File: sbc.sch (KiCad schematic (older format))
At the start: 1 part

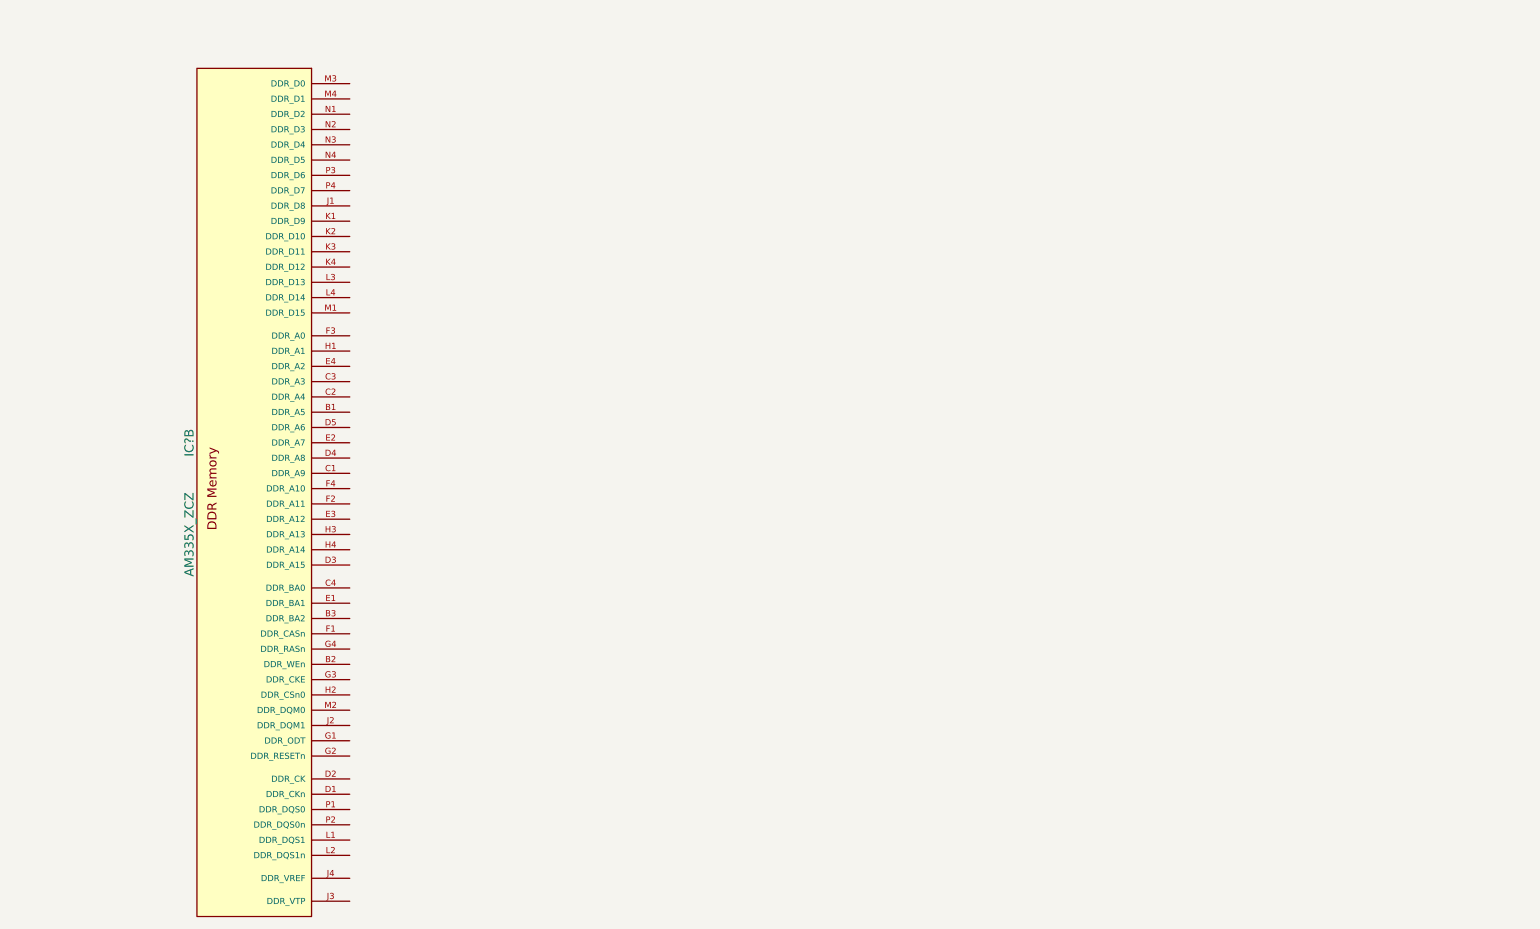
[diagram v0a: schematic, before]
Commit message: Connected micro SD
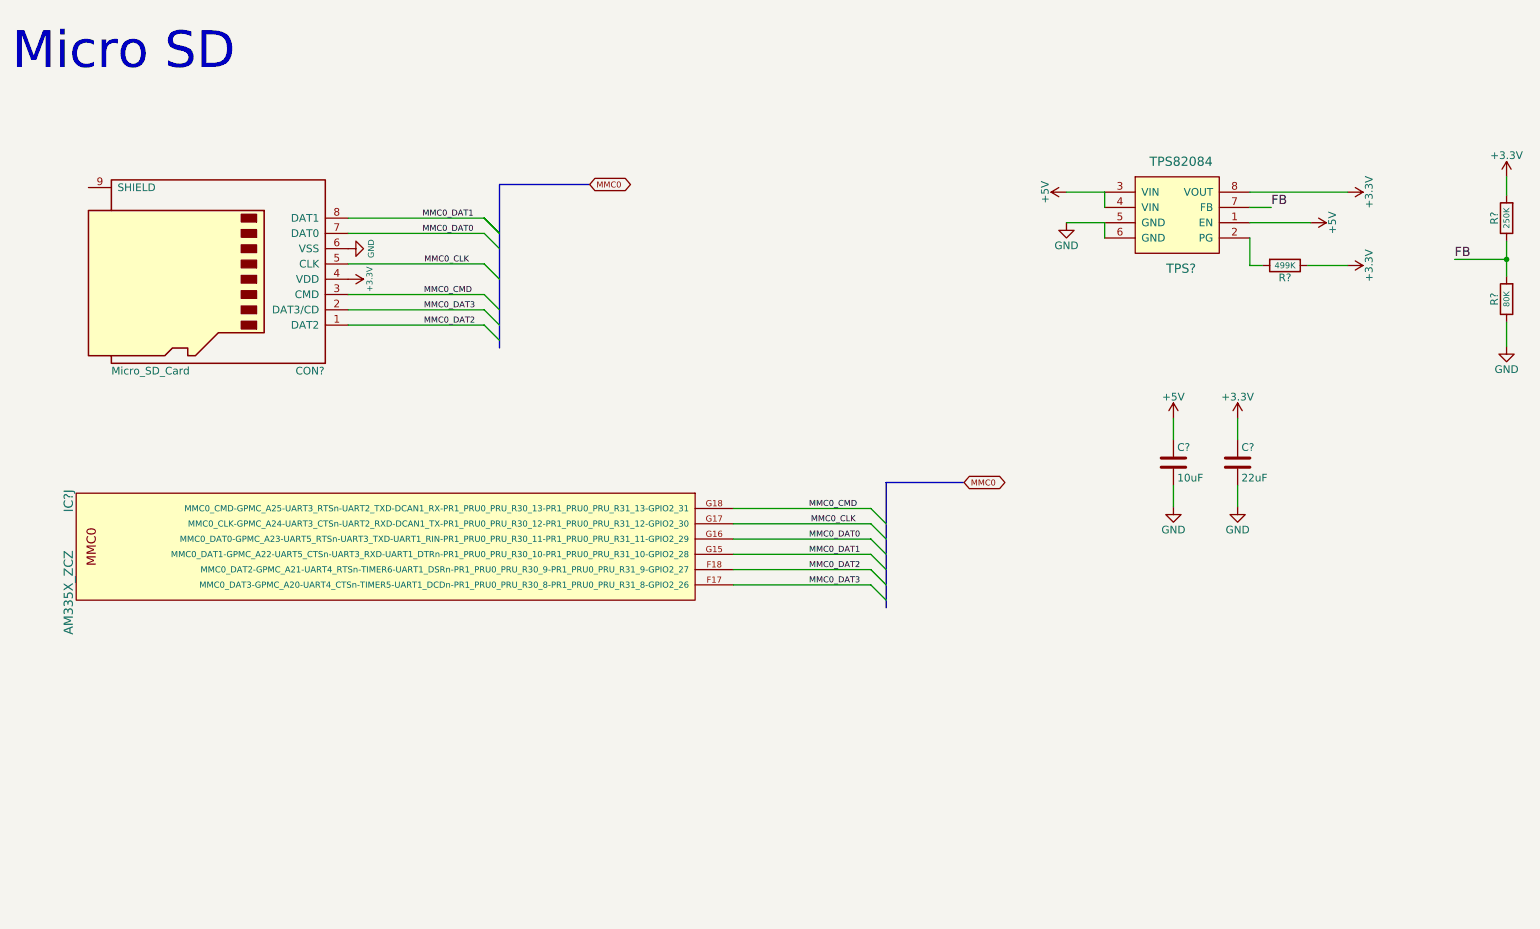
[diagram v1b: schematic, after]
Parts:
- removed IC?: AM335X_ZCZ, symbol AM335X_ZCZ
- added C?: 10uF, symbol C
- added C?: 22uF, symbol C
- added CON?: Micro_SD_Card, symbol Micro_SD_Card
- added IC?: AM335X_ZCZ, symbol AM335X_ZCZ
- added R?: 499K, symbol R
- added R?: 250K, symbol R
- added R?: 80K, symbol R
- added TPS?: TPS82084, symbol TPS82084
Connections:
- new net: R?.2, TPS?.2 (PG)
- new net +3V3: C?.1, CON?.4 (VDD), R?.1, R?.2, TPS?.8 (VOUT)
- new net +5V: C?.1, TPS?.1 (EN), TPS?.3 (VIN), TPS?.4 (VIN)
- new net FB: R?.1, R?.2, TPS?.7 (FB)
- new net GND: C?.2, C?.2, CON?.6 (VSS), R?.1, TPS?.5 (GND), TPS?.6 (GND)
- new net MMC0_CLK: CON?.5 (CLK), IC?.G17 (MMC0_CLK-GPMC_A24-UART3_CTSn-UART2_RXD-DCAN1_TX-PR1_PRU0_PRU_R30_12-PR1_PRU0_PRU_R31_12-GPIO2_30)
- new net MMC0_CMD: CON?.3 (CMD), IC?.G18 (MMC0_CMD-GPMC_A25-UART3_RTSn-UART2_TXD-DCAN1_RX-PR1_PRU0_PRU_R30_13-PR1_PRU0_PRU_R31_13-GPIO2_31)
- new net MMC0_DAT0: CON?.7 (DAT0), IC?.G16 (MMC0_DAT0-GPMC_A23-UART5_RTSn-UART3_TXD-UART1_RIN-PR1_PRU0_PRU_R30_11-PR1_PRU0_PRU_R31_11-GPIO2_29)
- new net MMC0_DAT1: CON?.8 (DAT1), IC?.G15 (MMC0_DAT1-GPMC_A22-UART5_CTSn-UART3_RXD-UART1_DTRn-PR1_PRU0_PRU_R30_10-PR1_PRU0_PRU_R31_10-GPIO2_28)
- new net MMC0_DAT2: CON?.1 (DAT2), IC?.F18 (MMC0_DAT2-GPMC_A21-UART4_RTSn-TIMER6-UART1_DSRn-PR1_PRU0_PRU_R30_9-PR1_PRU0_PRU_R31_9-GPIO2_27)
- new net MMC0_DAT3: CON?.2 (DAT3/CD), IC?.F17 (MMC0_DAT3-GPMC_A20-UART4_CTSn-TIMER5-UART1_DCDn-PR1_PRU0_PRU_R30_8-PR1_PRU0_PRU_R31_8-GPIO2_26)
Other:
- note added: "Micro SD"

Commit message: Connected RAM
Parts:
- added C?: 10uF, symbol C
- added C?: 22uF, symbol C
- added CON?: Micro_SD_Card, symbol Micro_SD_Card
- added DRAM?: DRAM-IS43TR16128B-125KBL, symbol DRAM-IS43TR16128B-125KBL
- added IC? (x2): AM335X_ZCZ, symbol AM335X_ZCZ
- added R?: 499K, symbol R
- added R?: 250K, symbol R
- added R?: 80K, symbol R
- added R?: 49.9, symbol R
- added TPS?: TPS82084, symbol TPS82084
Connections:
- net +3V3: now also C?.1, CON?.4 (VDD), R?.1, R?.2, TPS?.8 (VOUT)
- net +5V: now also C?.1, TPS?.1 (EN), TPS?.3 (VIN), TPS?.4 (VIN)
- net FB: now also R?.1, R?.2, TPS?.7 (FB)
- net GND: now also C?.2, C?.2, CON?.6 (VSS), DRAM?.B1 (VSSQ), DRAM?.E1 (VSS), DRAM?.G9 (VSSQ), DRAM?.T9 (VSS), R?.1, R?.2, TPS?.5 (GND), TPS?.6 (GND)
- net MMC0_CLK: now also CON?.5 (CLK), IC?.G17 (MMC0_CLK-GPMC_A24-UART3_CTSn-UART2_RXD-DCAN1_TX-PR1_PRU0_PRU_R30_12-PR1_PRU0_PRU_R31_12-GPIO2_30)
- net MMC0_CMD: now also CON?.3 (CMD), IC?.G18 (MMC0_CMD-GPMC_A25-UART3_RTSn-UART2_TXD-DCAN1_RX-PR1_PRU0_PRU_R30_13-PR1_PRU0_PRU_R31_13-GPIO2_31)
- net MMC0_DAT0: now also CON?.7 (DAT0), IC?.G16 (MMC0_DAT0-GPMC_A23-UART5_RTSn-UART3_TXD-UART1_RIN-PR1_PRU0_PRU_R30_11-PR1_PRU0_PRU_R31_11-GPIO2_29)
- net MMC0_DAT1: now also CON?.8 (DAT1), IC?.G15 (MMC0_DAT1-GPMC_A22-UART5_CTSn-UART3_RXD-UART1_DTRn-PR1_PRU0_PRU_R30_10-PR1_PRU0_PRU_R31_10-GPIO2_28)
- net MMC0_DAT2: now also CON?.1 (DAT2), IC?.F18 (MMC0_DAT2-GPMC_A21-UART4_RTSn-TIMER6-UART1_DSRn-PR1_PRU0_PRU_R30_9-PR1_PRU0_PRU_R31_9-GPIO2_27)
- net MMC0_DAT3: now also CON?.2 (DAT3/CD), IC?.F17 (MMC0_DAT3-GPMC_A20-UART4_CTSn-TIMER5-UART1_DCDn-PR1_PRU0_PRU_R30_8-PR1_PRU0_PRU_R31_8-GPIO2_26)
- net at CON?.9 (SHIELD): now also CON?.9 (SHIELD)
- net at R?.2, TPS?.2 (PG): now also R?.2, TPS?.2 (PG)
- new net: IC?.J3 (DDR_VTP), R?.1
- new net +1.5V: DRAM?.A1 (VDDQ), DRAM?.H9 (VDDQ), DRAM?.N1 (VDD), DRAM?.R9 (VDD)
- new net DDR_A0: DRAM?.N3 (A0), IC?.F3 (DDR_A0)
- new net DDR_A1: DRAM?.P7 (A1), IC?.H1 (DDR_A1)
- new net DDR_A10: DRAM?.L7 (A10/AP), IC?.F4 (DDR_A10)
- new net DDR_A11: DRAM?.R7 (A11), IC?.F2 (DDR_A11)
- new net DDR_A12: DRAM?.N7 (A12/BC#), IC?.E3 (DDR_A12)
- new net DDR_A13: DRAM?.T3 (A13), IC?.H3 (DDR_A13)
- new net DDR_A2: DRAM?.P3 (A2), IC?.E4 (DDR_A2)
- new net DDR_A3: DRAM?.N2 (A3), IC?.C3 (DDR_A3)
- new net DDR_A4: DRAM?.P8 (A4), IC?.C2 (DDR_A4)
- new net DDR_A5: DRAM?.P2 (A5), IC?.B1 (DDR_A5)
- new net DDR_A6: DRAM?.R8 (A6), IC?.D5 (DDR_A6)
- new net DDR_A7: DRAM?.R2 (A7), IC?.E2 (DDR_A7)
- new net DDR_A8: DRAM?.T8 (A8), IC?.D4 (DDR_A8)
- new net DDR_A9: DRAM?.R3 (A9), IC?.C1 (DDR_A9)
- new net DDR_BA0: DRAM?.M2 (BA0), IC?.C4 (DDR_BA0)
- new net DDR_BA1: DRAM?.N8 (BA1), IC?.E1 (DDR_BA1)
- new net DDR_BA2: DRAM?.M3 (BA2), IC?.B3 (DDR_BA2)
- new net DDR_CASn: DRAM?.K3 (CAS#), IC?.F1 (DDR_CASn)
- new net DDR_CK: DRAM?.J7 (CK), IC?.D2 (DDR_CK)
- new net DDR_CKE: DRAM?.K9 (CKE), IC?.G3 (DDR_CKE)
- new net DDR_CKn: DRAM?.K7 (CK#), IC?.D1 (DDR_CKn)
- new net DDR_CSn0: DRAM?.L2 (CS#), IC?.H2 (DDR_CSn0)
- new net DDR_D0: DRAM?.E3 (DQL0), IC?.M3 (DDR_D0)
- new net DDR_D1: DRAM?.F7 (DQL1), IC?.M4 (DDR_D1)
- new net DDR_D10: DRAM?.C8 (DQU2), IC?.K2 (DDR_D10)
- new net DDR_D11: DRAM?.C2 (DQU3), IC?.K3 (DDR_D11)
- new net DDR_D12: DRAM?.A7 (DQU4), IC?.K4 (DDR_D12)
- new net DDR_D13: DRAM?.A2 (DQU5), IC?.L3 (DDR_D13)
- new net DDR_D14: DRAM?.B8 (DQU6), IC?.L4 (DDR_D14)
- new net DDR_D15: DRAM?.A3 (DQU7), IC?.M1 (DDR_D15)
- new net DDR_D2: DRAM?.F2 (DQL2), IC?.N1 (DDR_D2)
- new net DDR_D3: DRAM?.F8 (DQL3), IC?.N2 (DDR_D3)
- new net DDR_D4: DRAM?.H3 (DQL4), IC?.N3 (DDR_D4)
- new net DDR_D5: DRAM?.H8 (DQL5), IC?.N4 (DDR_D5)
- new net DDR_D6: DRAM?.G2 (DQL6), IC?.P3 (DDR_D6)
- new net DDR_D7: DRAM?.H7 (DQL7), IC?.P4 (DDR_D7)
- new net DDR_D8: DRAM?.D7 (DQU0), IC?.J1 (DDR_D8)
- new net DDR_D9: DRAM?.C3 (DQU1), IC?.K1 (DDR_D9)
- new net DDR_DQM0: DRAM?.E7 (DML), IC?.M2 (DDR_DQM0)
- new net DDR_DQM1: DRAM?.D3 (DMU), IC?.J2 (DDR_DQM1)
- new net DDR_DQS0: DRAM?.F3 (DQSL), IC?.P1 (DDR_DQS0)
- new net DDR_DQS1: DRAM?.C7 (DQSU), IC?.L1 (DDR_DQS1)
- new net DDR_DQSn0: DRAM?.G3 (DQSL#), IC?.P2 (DDR_DQS0n)
- new net DDR_DQSn1: DRAM?.B7 (DQSU#), IC?.L2 (DDR_DQS1n)
- new net DDR_ODT: DRAM?.K1 (ODT), IC?.G1 (DDR_ODT)
- new net DDR_RASn: DRAM?.J3 (RAS#), IC?.G4 (DDR_RASn)
- new net DDR_RESETn: DRAM?.T2 (RESET#), IC?.G2 (DDR_RESETn)
- new net DDR_VREF: DRAM?.H1 (VREFDQ), DRAM?.M8 (VREFCA), IC?.J4 (DDR_VREF)
- new net DDR_WEn: DRAM?.L3 (WE#), IC?.B2 (DDR_WEn)
- new net DDR_ZQ: DRAM?.L8 (ZQ)
- no-connect marks 0 -> 8
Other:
- moved on the sheet: C?, CON?, IC?J, R?, TPS?

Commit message: Added Power, USB, System
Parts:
- removed C? (x2): 10uF, symbol C
- removed C? (x2): 22uF, symbol C
- removed CON?: Micro_SD_Card, symbol Micro_SD_Card
- removed IC?: AM335X_ZCZ, symbol AM335X_ZCZ
- removed R? (x2): 499K, symbol R
- removed R? (x2): 250K, symbol R
- removed R? (x2): 80K, symbol R
- removed TPS? (x2): TPS82084, symbol TPS82084
- added C? (x4): 0.1uF, symbol C
- added C? (x3): 10uF, symbol C
- added C? (x3): 22uF, symbol C
- added C? (x2): 24pF, symbol C
- added C? (x2): 25pF, symbol C
- added C? (x4): 1uF, symbol C
- added F?: Polyfuse, symbol Polyfuse
- added IC? (x3): AM335X_ZCZ, symbol AM335X_ZCZ
- added L?: Ferrite_Bead, symbol Ferrite_Bead
- added P?: USB_A, symbol USB_A
- added R? (x2): 1K, symbol R
- added R? (x3): 499K, symbol R
- added R?: 70K, symbol R
- added R? (x3): 80K, symbol R
- added R?: 250K, symbol R
- added R?: 30K, symbol R
- added R?: 240, symbol R
- added R?: 1M, symbol R
- added R?: 10K, symbol R
- added TPS? (x3): TPS82084, symbol TPS82084
- added Y?: 24MHz, symbol Crystal
- added Y?: 32.768KHz, symbol Crystal
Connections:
- net +1.5V: now also C?.1, C?.1, R?.1, R?.1, R?.1, TPS?.8 (VOUT)
- net +3V3: now also C?.1, IC?.N15 (VDDA3P3V_USB0), IC?.R15 (xVDDA3P3V_USB1), R?.1, R?.1, TPS?.8 (VOUT)
- net +5V: now also C?.1, C?.1, C?.1, IC?.F16 (USB0_DRVVBUS-GPIO0_18), IC?.P15 (USB0_VBUS), L?.1, TPS?.1 (EN), TPS?.1 (EN), TPS?.1 (EN), TPS?.3 (VIN), TPS?.3 (VIN), TPS?.3 (VIN), TPS?.4 (VIN), TPS?.4 (VIN), TPS?.4 (VIN)
- net DDR_VREF: now also C?.1, C?.1, C?.1, C?.2, R?.1, R?.2
- net DDR_ZQ: now also R?.2
- net GND: now also C?.2, C?.2, C?.2, C?.2, C?.2, C?.2, C?.2, C?.2, C?.2, C?.2, C?.2, C?.2, C?.2, IC?.A1 (VSS), IC?.A18 (VSS), IC?.F8 (VSS), IC?.G11 (VSS), IC?.G12 (VSS), IC?.G8 (VSS), IC?.G9 (VSS), IC?.H10 (VSS), IC?.H12 (VSS), IC?.H6 (VSS), IC?.H7 (VSS), IC?.H8 (VSS), IC?.H9 (VSS), IC?.J10 (VSS), IC?.J11 (VSS), IC?.J6 (VSS), IC?.J7 (VSS), IC?.J8 (VSS), IC?.J9 (VSS), IC?.K10 (VSS), IC?.K11 (VSS), IC?.K7 (VSS), IC?.K9 (VSS), IC?.L10 (VSS), IC?.L11 (VSS), IC?.L12 (VSS), IC?.L13 (VSS), IC?.M10 (VSS), IC?.M12 (VSS), IC?.M14 (VSSA_USB), IC?.M6 (VSS), IC?.M7 (VSS), IC?.M8 (VSS), IC?.M9 (VSS), IC?.N10 (VSS), IC?.N11 (VSS), IC?.N14 (VSSA_USB), IC?.N7 (VSS), IC?.V1 (VSS), IC?.V18 (VSS), P?.4 (GND), R?.1, R?.2, R?.2, R?.2, R?.2, R?.2, TPS?.5 (GND), TPS?.5 (GND), TPS?.5 (GND), TPS?.6 (GND), TPS?.6 (GND), TPS?.6 (GND)
- new net: F?.2, P?.1 (VBUS)
- new net: C?.1, IC?.C10 (CAP_VBB_MPU)
- new net: C?.1, IC?.D11 (CAP_VDD_SRAM_MPU)
- new net: C?.1, IC?.D6 (CAP_VDD_RTC)
- new net: C?.1, IC?.D9 (CAP_VDD_SRAM_CORE)
- new net: F?.1, L?.2
- new net: R?.2, TPS?.2 (PG) (x3)
- new net: C?.1, IC?.A4 (RTC_XTALOUT), Y?.2
- new net: C?.1, IC?.A6 (RTC_XTALIN), Y?.1
- new net: IC?.B4 (RTC_KALDO_ENn), R?.1
- new net: C?.1, IC?.U11 (XTALOUT), R?.2, Y?.2
- new net: C?.1, IC?.V10 (XTALIN), R?.1, Y?.1
- new net 1.1FB: R?.1, R?.2, TPS?.7 (FB)
- new net 1.1V: C?.1, IC?.A2 (xVDD_MPU_MON), IC?.F10 (xVDD_MPU), IC?.F11 (xVDD_MPU), IC?.F12 (xVDD_MPU), IC?.F13 (xVDD_MPU), IC?.F6 (VDD_CORE), IC?.F7 (VDD_CORE), IC?.G10 (VDD_CORE), IC?.G13 (xVDD_MPU), IC?.G6 (VDD_CORE), IC?.G7 (VDD_CORE), IC?.H11 (VDD_CORE), IC?.H13 (xVDD_MPU), IC?.J12 (VDD_CORE), IC?.J13 (xVDD_MPU), IC?.K12 (VDD_CORE), IC?.K6 (VDD_CORE), IC?.K8 (VDD_CORE), IC?.L6 (VDD_CORE), IC?.L7 (VDD_CORE), IC?.L8 (VDD_CORE), IC?.L9 (VDD_CORE), IC?.M11 (VDD_CORE), IC?.M13 (VDD_CORE), IC?.N12 (VDD_CORE), IC?.N13 (VDD_CORE), IC?.N8 (VDD_CORE), IC?.N9 (VDD_CORE), R?.1, R?.1, TPS?.8 (VOUT)
- new net 1.5FB: R?.1, R?.2, TPS?.7 (FB)
- new net 1.5V: IC?.E5 (VDDS_DDR), IC?.F5 (VDDS_DDR), IC?.G5 (VDDS_DDR), IC?.H5 (VDDS_DDR), IC?.J5 (VDDS_DDR), IC?.K5 (VDDS_DDR), IC?.L5 (VDDS_DDR)
- new net 1.8V: IC?.D10 (VDDS_SRAM_MPU_BB), IC?.D7 (VDDS_RTC), IC?.D8 (VDDA_ADC), IC?.E14 (VDDS), IC?.E6 (VDDS), IC?.E7 (VDDS_PLL_DDR), IC?.E9 (VDDS_SRAM_CORE_BG), IC?.F9 (VDDS), IC?.H15 (VDDS_PLL_MPU), IC?.K13 (VDDS), IC?.N16 (VDDA1P8V_USB0), IC?.N6 (VDDS), IC?.P14 (VDDS), IC?.P9 (VDDS), IC?.R10 (VDDS_PLL_CORE_LCD), IC?.R11 (VDDS_OSC), IC?.R16 (xVDDA1P8V_USB1)
- new net 3.3FB: R?.1, R?.2, TPS?.7 (FB)
- new net GND_OSC0: C?.2, C?.2, IC?.V11 (VSS_OSC)
- new net GND_OSC1: C?.2, C?.2, IC?.A5 (xVSS_RTC)
- new net USBD+: IC?.N17 (USB0_DP), P?.2 (D-)
- new net USBD-: IC?.N18 (USB0_DM), P?.3 (D+)
- no-connect marks 8 -> 34
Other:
- note added: "Device Port"
- note added: "Power Rails"
- note added: "Processor Power"
- note added: "RAM"
- note added: "System"
- moved on the sheet: CON?, DRAM?, IC?B, IC?J, R?

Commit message: Schematic completed
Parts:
- added C? (x18): 10nF, symbol C
- added C? (x8): 10uF, symbol C
- added C? (x10): 1uF, symbol C
- added C?: 22uF, symbol C
- added IC?: AM335X_ZCZ, symbol AM335X_ZCZ
- added L?: 10OHM600mA, symbol Ferrite_Bead
- added L? (x3): Ferrite_Bead, symbol Ferrite_Bead
- added R? (x6): 10K, symbol R
- added R?: 499K, symbol R
- added R?: 100K, symbol R
- added R?: 80K, symbol R
- added TPS?: TPS82084, symbol TPS82084
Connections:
- net 1.5V is gone; now on net +1.5V: IC?.E5 (VDDS_DDR), IC?.F5 (VDDS_DDR), IC?.G5 (VDDS_DDR), IC?.H5 (VDDS_DDR), IC?.J5 (VDDS_DDR), IC?.K5 (VDDS_DDR), IC?.L5 (VDDS_DDR)
- net +1.5V: now also C?.1, C?.1, C?.1, C?.1, C?.1, C?.1, C?.1, C?.1, C?.1, C?.1, C?.1, C?.2, C?.2, C?.2, L?.1; no longer TPS?.8 (VOUT)
- net +3V3: now also IC?.E10 (VDDSHV6), IC?.E11 (VDDSHV6), IC?.E12 (VDDSHV6), IC?.E13 (VDDSHV6), IC?.F14 (VDDSHV6), IC?.G14 (VDDSHV6), IC?.H14 (VDDSHV4), IC?.J14 (VDDSHV4), IC?.K14 (VDDSHV5), IC?.L14 (VDDSHV5), IC?.N5 (VDDSHV6), IC?.P10 (VDDSHV2), IC?.P11 (VDDSHV2), IC?.P12 (VDDSHV3), IC?.P13 (VDDSHV3), IC?.P5 (VDDSHV6), IC?.P6 (VDDSHV6), IC?.P7 (VDDSHV1), IC?.P8 (VDDSHV1), C?.1, C?.1, C?.1, C?.1, C?.1, C?.1, C?.2, L?.1, R?.1, R?.1, R?.1, R?.1, R?.1, R?.1; no longer TPS?.8 (VOUT)
- net +5V: now also C?.1, TPS?.1 (EN), TPS?.3 (VIN), TPS?.4 (VIN); no longer IC?.F16 (USB0_DRVVBUS-GPIO0_18)
- net 1.1V: now also C?.1, C?.1, C?.1, C?.1, C?.1, C?.1, C?.1, C?.1, C?.2, L?.1; no longer TPS?.8 (VOUT)
- net 1.8V: now also C?.1, C?.1, C?.1, C?.1, C?.1, C?.2, L?.1, R?.1, R?.1; no longer IC?.D8 (VDDA_ADC), IC?.E9 (VDDS_SRAM_CORE_BG)
- net GND: now also IC?.A9 (VREFN), IC?.B9 (VREFP), IC?.D8 (VDDA_ADC), IC?.E8 (VSSA_ADC), C?.1, C?.1, C?.1, C?.1, C?.1, C?.1, C?.2, C?.2, C?.2, C?.2, C?.2, C?.2, C?.2, C?.2, C?.2, C?.2, C?.2, C?.2, C?.2, C?.2, C?.2, C?.2, C?.2, C?.2, C?.2, C?.2, C?.2, C?.2, C?.2, C?.2, C?.2, C?.2, C?.2, C?.2, C?.2, C?.2, C?.2, IC?.A7 (AIN3), IC?.A8 (AIN6), IC?.B6 (AIN0), IC?.B7 (AIN2), IC?.B8 (AIN5), IC?.C7 (AIN1), IC?.C8 (AIN4), IC?.C9 (AIN7), R?.2, TPS?.5 (GND), TPS?.6 (GND)
- net MMC0_CLK: now also R?.2
- net MMC0_CMD: now also R?.2
- net MMC0_DAT0: now also R?.2
- net MMC0_DAT1: now also R?.2
- net MMC0_DAT2: now also R?.2
- net MMC0_DAT3: now also R?.2
- new net: L?.2, TPS?.8 (VOUT) (x4)
- new net: R?.2, TPS?.2 (PG)
- new net 1.8FB: R?.1, R?.2, TPS?.7 (FB)
- no-connect marks 34 -> 35
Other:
- note added: "Unused ADC\n"
- moved on the sheet: C?, CON?, DRAM?, F?, IC?B, IC?C, IC?J, IC?K, L?, P?, R?, TPS?

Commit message: Fixed errors
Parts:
- gave numbers to parts that had none: 95
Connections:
- net +1.5V: now also DRAM1.B2 (VDD), DRAM1.D9 (VDD), DRAM1.G7 (VDD), DRAM1.K2 (VDD), DRAM1.K8 (VDD), DRAM1.N9 (VDD), DRAM1.R1 (VDD); no longer DRAM1.H9 (VDDQ)
- net 1.8V: now also IC1.E9 (VDDS_SRAM_CORE_BG)
- net GND: now also DRAM1.A9 (VSS), DRAM1.B3 (VSS), DRAM1.B9 (VSSQ), DRAM1.D1 (VSSQ), DRAM1.D8 (VSSQ), DRAM1.E2 (VSSQ), DRAM1.E8 (VSSQ), DRAM1.F9 (VSSQ), DRAM1.G1 (VSSQ), DRAM1.G8 (VSS), DRAM1.J2 (VSS), DRAM1.J8 (VSS), DRAM1.M1 (VSS), DRAM1.M9 (VSS), DRAM1.P1 (VSS), DRAM1.P9 (VSS), DRAM1.T1 (VSS)
- net at DRAM1.A8 (VDDQ): now also DRAM1.C1 (VDDQ), DRAM1.C9 (VDDQ), DRAM1.D2 (VDDQ), DRAM1.E9 (VDDQ), DRAM1.F1 (VDDQ), DRAM1.H2 (VDDQ), DRAM1.H9 (VDDQ)
- no-connect marks 35 -> 37

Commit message: Regualar backup commit
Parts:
- removed L1, L2, L4, L5: Ferrite_Bead, symbol Ferrite_Bead
- removed L3: 10OHM600mA, symbol Ferrite_Bead
- C1, C10, C11, C12, C13, C14, C15, C16, C17, C18, C19, C2, C20, C21, C22, C23, C24, C25, C26, C27, C28, C29, C3, C30, C31, C32, C33, C34, C35, C36, C37, C38, C39, C4, C40, C41, C42, C43, C44, C45, C46, C47, C48, C49, C5, C50, C51, C52, C53, C54, C55, C6, C7, C8, C9: footprint (none) -> Capacitors_SMD:C_0603_HandSoldering
- CON1: footprint (none) -> libraries:MICRO_SD_HINGE_AMP
- DRAM1: footprint (none) -> SMD_Packages:BGA-96_pitch0.8mm_dia0.4mm
- F1: footprint (none) -> Fuse_Holders_and_Fuses:Fuse_SMD1206_HandSoldering
- IC1: footprint (none) -> libraries:bga-csg324
- P1: footprint (none) -> Connectors:USB_A
- R1, R10, R11, R12, R13, R14, R15, R16, R17, R18, R19, R2, R20, R21, R22, R23, R24, R3, R4, R5, R6, R7, R8, R9: footprint (none) -> Resistors_SMD:R_0603_HandSoldering
- TPS1, TPS2, TPS3, TPS4: footprint (none) -> Housings_SSOP:MSOP-8-1EP_3x3mm_Pitch0.65mm
- Y1, Y2: footprint (none) -> Crystals:Crystal_SMD_0603-2pin_6.0x3.5mm_HandSoldering
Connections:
- net +1.5V: now also DRAM1.A8 (VDDQ), DRAM1.C1 (VDDQ), DRAM1.C9 (VDDQ), DRAM1.D2 (VDDQ), DRAM1.E9 (VDDQ), DRAM1.F1 (VDDQ), DRAM1.H2 (VDDQ), DRAM1.H9 (VDDQ), TPS4.8 (VOUT)
- net +3V3: now also TPS2.8 (VOUT)
- net +5V: now also F1.1
- net 1.1V: now also TPS1.8 (VOUT)
- net 1.8V: now also TPS3.8 (VOUT)

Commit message: Regular backup
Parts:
- Y1, Y2: footprint Crystals:Crystal_SMD_0603-2pin_6.0x3.5mm_HandSoldering -> Crystals:Crystal_SMD_2012-2pin_2.0x1.2mm_HandSoldering
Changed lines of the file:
@@
 F 0 "Y2" H 8250 12710 50  0000 C CNN
 F 1 "24MHz" H 8250 12410 50  0000 C CNN
-F 2 "Crystals:Crystal_SMD_0603-2pin_6.0x3.5mm_HandSoldering" H 8250 12560 50  0001 C CNN
+F 2 "Crystals:Crystal_SMD_2012-2pin_2.0x1.2mm_HandSoldering" H 8250 12560 50  0001 C CNN
 F 3 "" H 8250 12560 50  0000 C CNN
 	1    8250 12560
@@
 F 0 "Y1" H 6460 13160 50  0000 C CNN
 F 1 "32.768KHz" H 6370 12860 50  0000 C CNN
-F 2 "Crystals:Crystal_SMD_0603-2pin_6.0x3.5mm_HandSoldering" H 6460 13010 50  0001 C CNN
+F 2 "Crystals:Crystal_SMD_2012-2pin_2.0x1.2mm_HandSoldering" H 6460 13010 50  0001 C CNN
 F 3 "" H 6460 13010 50  0000 C CNN
 	1    6460 13010

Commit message: board design v1 almost complete
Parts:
- added R25: 10K, Resistors_SMD:R_0603_HandSoldering, symbol R
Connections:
- net +1.5V: now also R25.1
- net +3V3: now also C15.1; no longer C15.2
- net DDR_RESETn: now also R25.2
- net GND: now also C15.2; no longer C15.1
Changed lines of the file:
@@
 F 3 "" H 6020 5430 50  0000 C CNN
 	1    6020 5430
-	0    1    1    0
+	0    -1   -1   0
 $EndComp
 Wire Bus Line
@@
 	6170 4320 6310 4320
 Wire Wire Line
-	6170 4550 6310 4550
+	6310 4550 6170 4550
 Wire Wire Line
 	6310 4760 6170 4760
@@
 	6380 7930 6520 7930
 Wire Wire Line
-	6380 8160 6520 8160
+	6520 8160 6380 8160
 Wire Wire Line
 	6520 8370 6380 8370
@@
 	6840 9750 6980 9750
 Wire Wire Line
-	6840 9980 6980 9980
+	6980 9980 6840 9980
 Wire Wire Line
 	6980 10190 6840 10190
@@
 	7530 7930 7670 7930
 Wire Wire Line
-	7530 8160 7670 8160
+	7670 8160 7530 8160
 Wire Wire Line
 	7670 8370 7530 8370
@@
 NoConn ~ 16240 11330
 Connection ~ 16060 4290
+Wire Wire Line
+	17940 8360 18360 8360
+$Comp
+L R R25
+U 1 1 588DDA65
+P 18510 8360
+F 0 "R25" V 18590 8360 50  0000 C CNN
+F 1 "10K" V 18510 8360 50  0000 C CNN
+F 2 "Resistors_SMD:R_0603_HandSoldering" V 18440 8360 50  0001 C CNN
+F 3 "" H 18510 8360 50  0000 C CNN
+	1    18510 8360
+	0    1    1    0
+$EndComp
+Wire Wire Line
+	18660 8360 18890 8360
+$Comp
+L +1.5V #PWR079
+U 1 1 588DEB61
+P 18890 8360
+F 0 "#PWR079" H 18890 8500 20  0001 C CNN
+F 1 "+1.5V" H 18880 8520 60  0000 C CNN
+F 2 "" H 18890 8360 60  0001 C CNN
+F 3 "" H 18890 8360 60  0001 C CNN
+	1    18890 8360
+	0    1    1    0
+$EndComp
+Text Label 17940 8360 2    60   ~ 0
+DDR_RESETn
 $EndSCHEMATC
